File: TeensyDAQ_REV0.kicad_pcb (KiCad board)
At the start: 4 copper layers, 101.6 x 82.6 mm, 104 parts, among them U100 TPS56637RPAR, U101 INA226AIDGSR, U102 BNO055, U103 SN65HVD230DR, U104 DRV5032FBDBZR, Y100 ABS07-32.768KHZ-T

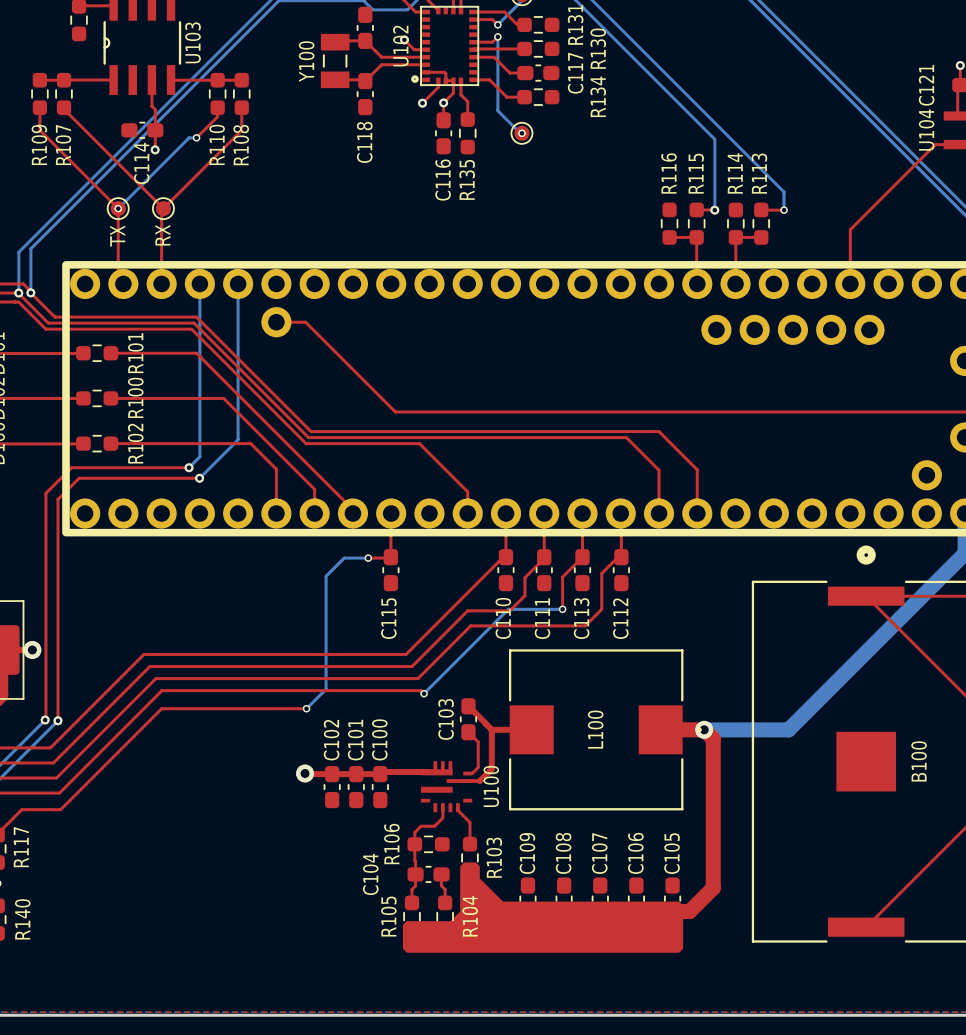
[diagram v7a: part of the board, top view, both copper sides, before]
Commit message: added 5V test point at caps
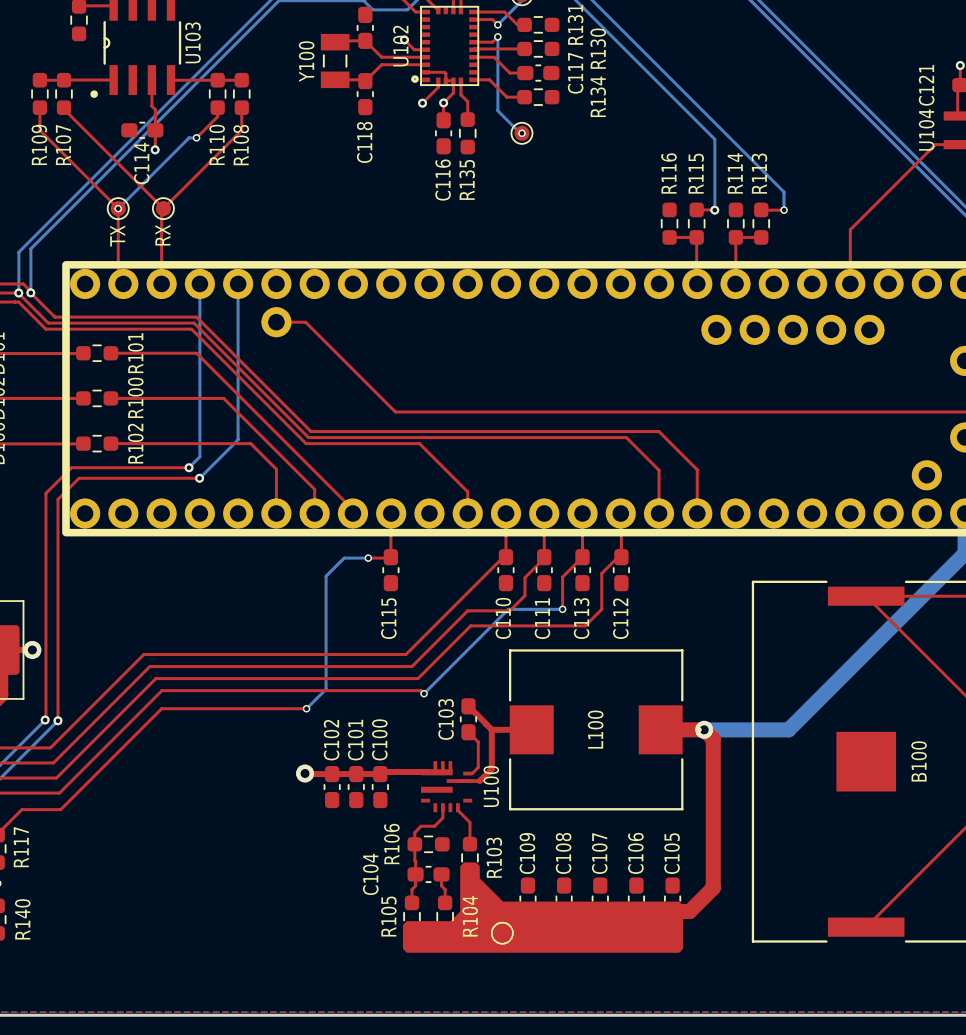
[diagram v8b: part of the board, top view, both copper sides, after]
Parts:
- added 5V103: TestPoint, TestPoint:TestPoint_Pad_D1.0mm, F.Cu at (164.7, 127.1)
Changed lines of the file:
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@@
 		(sheetfile "Teensy.kicad_sch")
 		(attr smd)
-		(fp_circle
-			(center -13.716 0.6731)
-			(end -13.335 0.6731)
-			(stroke
-				(width 0.508)
-				(type solid)
-			)
-			(fill none)
-			(layer "B.SilkS")
-		)
 		(fp_line
 			(start -11.938 8.1915)
@@
 			(layer "F.SilkS")
 		)
-		(fp_circle
-			(center -13.716 0.6731)
-			(end -13.335 0.6731)
-			(stroke
-				(width 0.508)
-				(type solid)
-			)
-			(fill none)
-			(layer "F.SilkS")
-		)
 		(fp_line
 			(start -12.065 8.3185)
@@
 		)
 	)
+	(footprint "TestPoint:TestPoint_Pad_D1.0mm"
+		(layer "F.Cu")
+		(at 164.7 127.1)
+		(descr "SMD pad as test Point, diameter 1.0mm")
+		(tags "test point SMD pad")
+		(property "Reference" "5V103"
+			(at 0 -1.448 0)
+			(layer "F.SilkS")
+			(hide yes)
+			(effects
+				(font
+					(size 1 1)
+					(thickness 0.15)
+				)
+			)
+		)
+		(property "Value" "TestPoint"
+			(at 0 1.55 0)
+			(layer "F.Fab")
+			(hide yes)
+			(effects
+				(font
+					(size 1 1)
+					(thickness 0.15)
+				)
+			)
+		)
+		(property "Footprint" "TestPoint:TestPoint_Pad_D1.0mm"
+			(at 0 0 0)
+			(unlocked yes)
+			(layer "F.Fab")
+			(hide yes)
+			(effects
+				(font
+					(size 1.27 1.27)
+					(thickness 0.15)
+				)
+			)
+		)
+		(property "Datasheet" ""
+			(at 0 0 0)
+			(unlocked yes)
+			(layer "F.Fab")
+			(hide yes)
+			(effects
+				(font
+					(size 1.27 1.27)
+					(thickness 0.15)
+				)
+			)
+		)
+		(property "Description" "test point"
+			(at 0 0 0)
+			(unlocked yes)
+			(layer "F.Fab")
+			(hide yes)
+			(effects
+				(font
+					(size 1.27 1.27)
+					(thickness 0.15)
+				)
+			)
+		)
+		(property ki_fp_filters "Pin* Test*")
+		(sheetname "Power Biasing")
+		(sheetfile "Power_Biasing.kicad_sch")
+		(attr exclude_from_pos_files)
+		(fp_circle
+			(center 0 0)
+			(end 0 0.7)
+			(stroke
+				(width 0.12)
+				(type solid)
+			)
+			(fill none)
+			(layer "F.SilkS")
+		)
+		(fp_circle
+			(center 0 0)
+			(end 1 0)
+			(stroke
+				(width 0.05)
+				(type solid)
+			)
+			(fill none)
+			(layer "F.CrtYd")
+		)
+		(fp_text user "${REFERENCE}"
+			(at 0 -1.45 0)
+			(layer "F.Fab")
+			(effects
+				(font
+					(size 1 1)
+					(thickness 0.15)
+				)
+			)
+		)
+		(pad "1" smd circle
+			(at 0 0)
+			(size 1 1)
+			(layers "F.Cu" "F.Mask")
+			(net 3 "+5V")
+			(pinfunction "1")
+			(pintype "passive")
+		)
+	)
 	(footprint "INA226AIDGSR:INA226AIDGSR"
 		(layer "F.Cu")
@@
 		(tags "test point SMD pad")
 		(property "Reference" "VD_1"
-			(at 1.75 -0.1 270)
+			(at 1.75 -0.1 -90)
 			(layer "B.SilkS")
 			(effects
@@
 		(net 3)
 	)
+	(gr_circle
+		(center 137.6 71.4)
+		(end 137.8 71.4)
+		(stroke
+			(width 0.1)
+			(type solid)
+		)
+		(fill solid)
+		(layer "F.SilkS")
+	)
 	(gr_rect
